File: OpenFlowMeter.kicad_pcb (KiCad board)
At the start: 2 copper layers, 70 x 28 mm, 92 parts, among them J1 Screw_Terminal_01x02, J2 Screw_Terminal_01x02, J3 Conn_01x06, J4 Conn_02x03_Odd_Even, J5 Conn_01x03, J6 Conn_02x04_Odd_Even, Q1 BC856, Q2 BC856, U1 LT1492, U2 STM32F103C8Tx, U3 LT1492, U4 R-78C3.3-1.0, U5 SN65HVD231, U6 LT1492, Y1 12 MHz

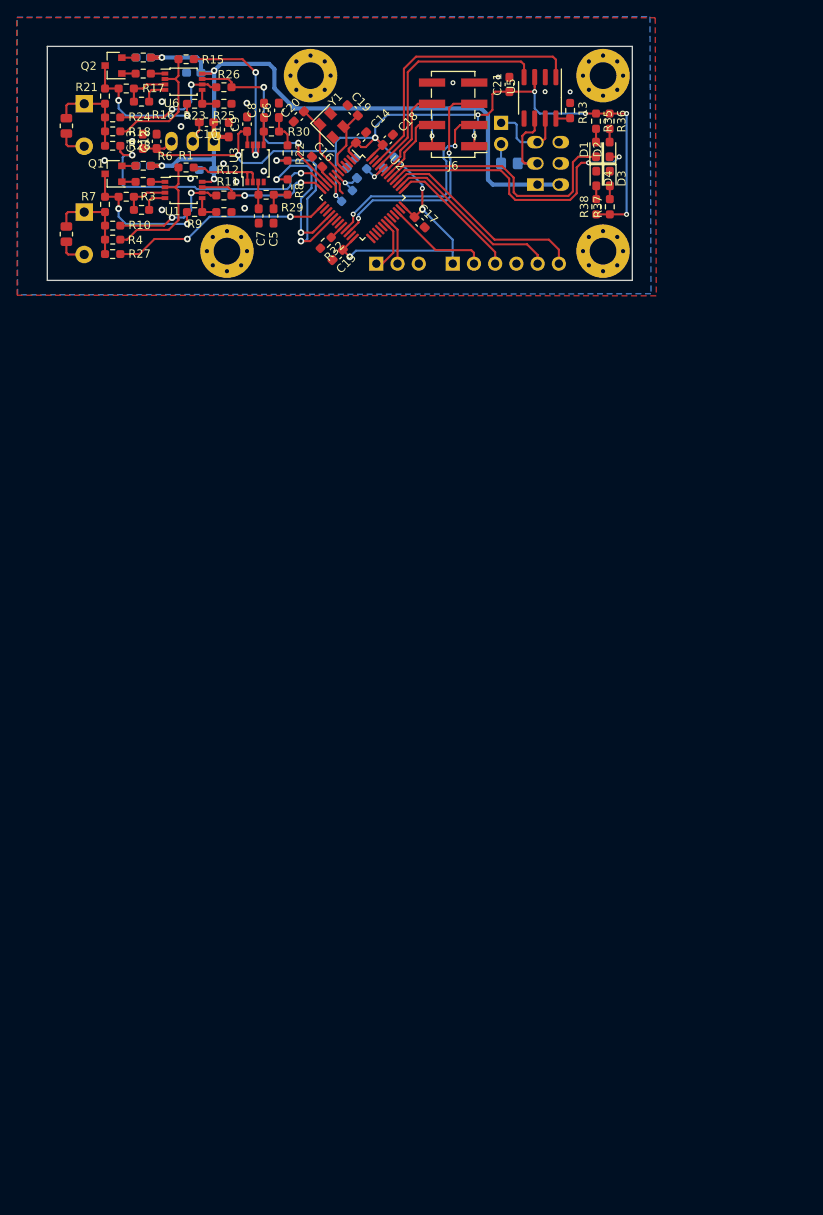
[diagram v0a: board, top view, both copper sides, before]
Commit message: BUGFIX footprint of LT1490
Footprint of LT1490 is SOIC8 and not Micro 8 -> had to enlarge the board.
At the same step, changed all footprints from handsolder to normal solder. (saves a little space)
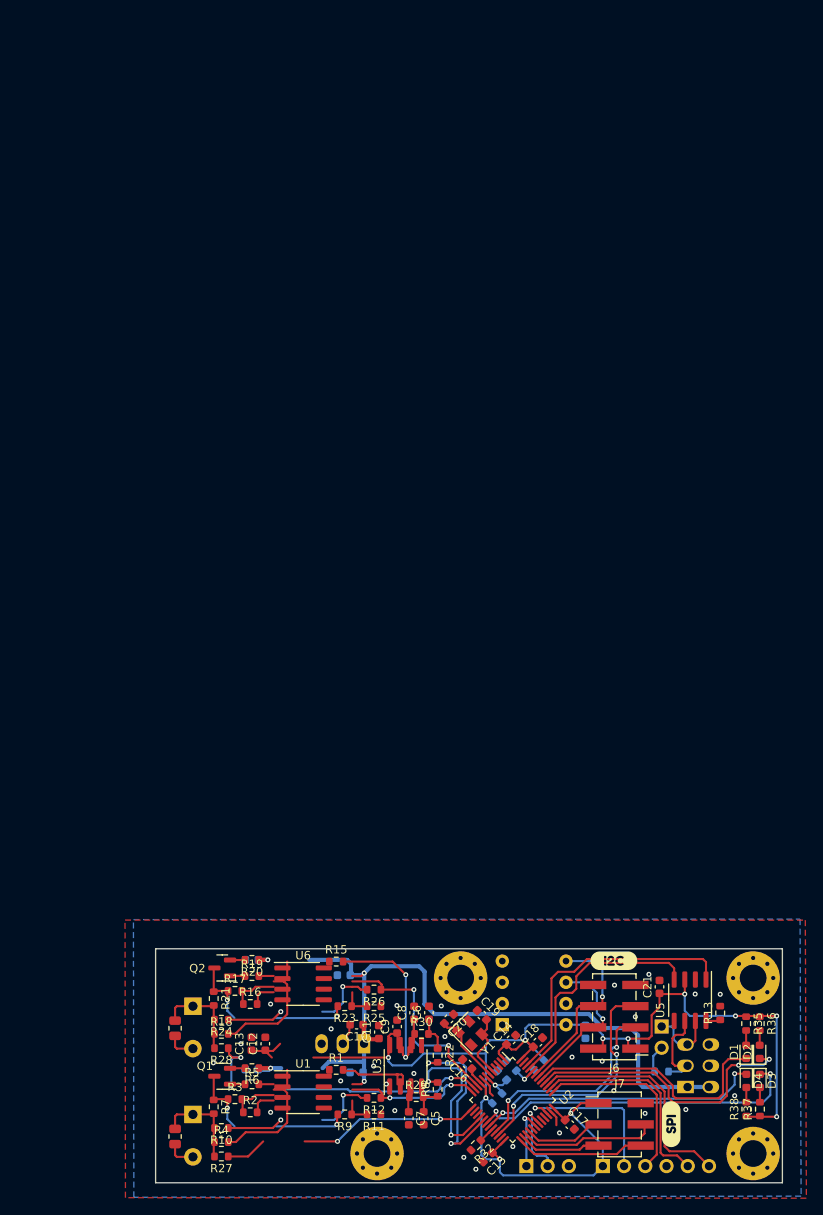
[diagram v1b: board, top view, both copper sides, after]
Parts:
- added C23: 100n, Capacitor_SMD:C_0603_1608Metric, B.Cu at (167.6, 92.7)
- added J7: Conn_02x03_Odd_Even, Connector_PinHeader_2.54mm:PinHeader_2x03_P2.54mm_Vertical_SMD, F.Cu at (171.7, 103.8)
- added U7: 24LC64, Package_DIP:DIP-8_W7.62mm, B.Cu at (157.6, 91.9)
- added kibuzzard-61DDB483: G***, kibuzzard-61DDB483, B.Cu at (173.6, 93.1)
- added kibuzzard-61DDB4E3: G***, kibuzzard-61DDB4E3, F.Cu at (177.8, 103.8)
- added kibuzzard-61DDB4F7: G***, kibuzzard-61DDB4F7, F.Cu at (171.0, 84.2)
- C1, C10, C11, C12, C13, C14, C15, C16, C17, C18, C19, C2, C20, C21, C22, C3, C4, C5, C6, C7, C8, C9: footprint Capacitor_SMD:C_0603_1608Metric_Pad1.08x0.95mm_HandSolder -> Capacitor_SMD:C_0603_1608Metric
- D1, D2, D3, D4: footprint LED_SMD:LED_0603_1608Metric_Pad1.05x0.95mm_HandSolder -> LED_SMD:LED_0603_1608Metric
- R1, R10, R11, R12, R13, R15, R16, R17, R18, R19, R2, R20, R21, R22, R23, R24, R25, R26, R27, R28, R29, R3, R30, R31, R32, R33, R34, R35, R36, R37, R38, R4, R5, R6, R7, R8, R9: footprint Resistor_SMD:R_0603_1608Metric_Pad0.98x0.95mm_HandSolder -> Resistor_SMD:R_0603_1608Metric
- R14: footprint Resistor_SMD:R_0805_2012Metric_Pad1.20x1.40mm_HandSolder -> Resistor_SMD:R_0603_1608Metric
- U1, U3, U6: footprint Package_SO:OnSemi_Micro8 -> Package_SO:SOIC-8_3.9x4.9mm_P1.27mm
- moved R14 110.2 mm to (176.7, 97.5)
- moved Y1 109.8 mm to (153.8, 92.8)
- moved JP1 109.8 mm to (176.7, 92.1)
- moved J6 109.7 mm to (171.0, 90.9)
- moved C10 109.5 mm to (140.2, 91.8)
- moved C14 109.5 mm to (158.7, 93.7)
- moved C15 109.5 mm to (155.9, 107.7)
- moved C16 109.5 mm to (153.4, 96.6)
- moved C2 109.5 mm to (140.2, 97.6)
- moved C20 109.5 mm to (151.2, 91.2), turned to -135 degrees
- moved C22 109.5 mm to (157.6, 97.9)
- moved C4 109.5 mm to (138.7, 85.9)
- moved C9 109.5 mm to (145.0, 92.1)
- moved D1 109.5 mm to (186.8, 95.1)
- moved D2 109.5 mm to (188.4, 95.1)
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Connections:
- D3 pad 1: unconnected-(D3-Pad1) -> /Controller/LED3
- D4 pad 1: unconnected-(D4-Pad1) -> /Controller/LED4
- U2 pad 18: unconnected-(U2-Pad18) -> /Controller/LED3
- U2 pad 19: unconnected-(U2-Pad19) -> /Controller/LED4
- U2 pad 25: unconnected-(U2-Pad25) -> /Controller/SPI_NSS
- U2 pad 26: unconnected-(U2-Pad26) -> /Controller/SPI_SCK
- U2 pad 27: unconnected-(U2-Pad27) -> /Controller/SPI_MISO
- U2 pad 28: unconnected-(U2-Pad28) -> /Controller/SPI_MOSI
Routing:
- net /Controller/LED3: track 0.00 -> 40.3 mm, vias 0 -> 2
- net /Controller/LED4: track 0.00 -> 34.1 mm, vias 0 -> 2
- net +3V3: track 157.1 -> 189.0 mm
- net /ISET 2: track 20.6 -> 0.00 mm, vias 2 -> 0
- net /Controller/SPI_MISO: track 0.00 -> 16.2 mm
- net /Controller/SPI_NSS: track 0.00 -> 15.9 mm
- net /Controller/I2C1_SDA: track 11.4 -> 22.1 mm, vias 0 -> 1
- net /Controller/SPI_SCK: track 0.00 -> 10.2 mm
- net /Controller/I2C1_SCL: track 9.01 -> 19.0 mm, vias 0 -> 1
- net /Controller/SPI_MOSI: track 0.00 -> 9.90 mm
- net /Controller/TMS_SWDIO: track 12.5 -> 19.2 mm, vias 0 -> 1
- net /Controller/TCK_SWCLK: track 16.2 -> 22.4 mm
- net /Controller/UART1_RX: track 5.58 -> 9.36 mm, vias 0 -> 1
- net /Controller/TDI: track 21.7 -> 25.3 mm
- net Net-(C8-Pad1): track 3.39 -> 0.00 mm
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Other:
- board size 70 x 28 mm -> 75 x 28 mm

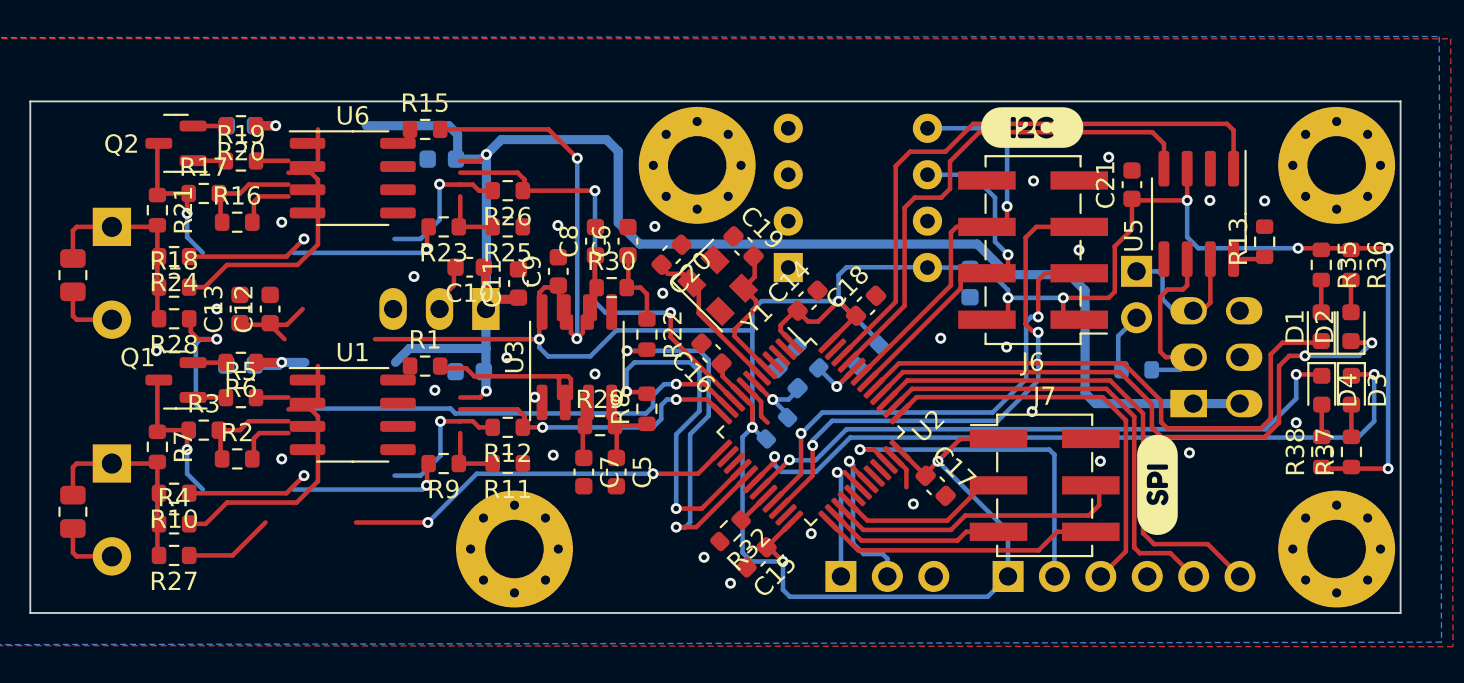
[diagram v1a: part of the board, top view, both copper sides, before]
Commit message: fixed layout
Fixed layout to host lager amplifier footprints.
Still some DRC warnings, but mostly regarding Silkscreen / Soldermask issues.
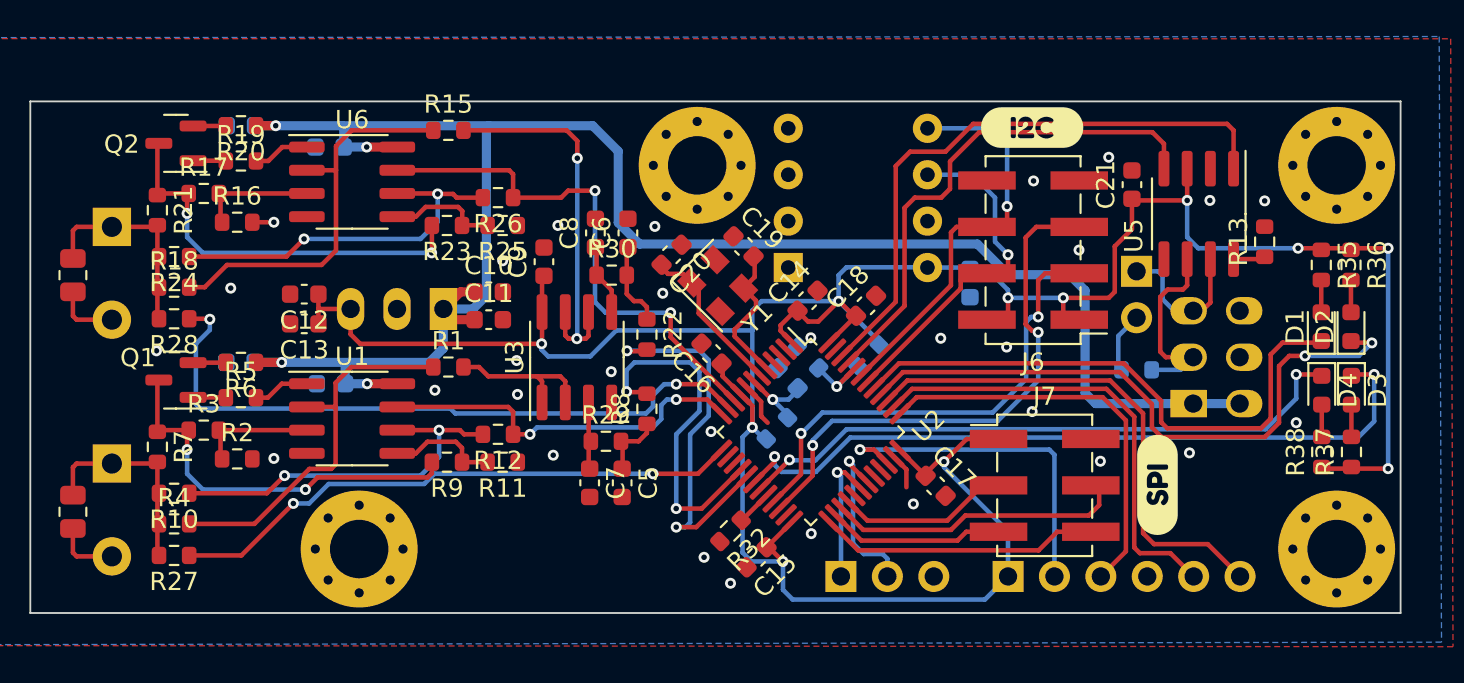
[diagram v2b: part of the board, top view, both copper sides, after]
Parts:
- moved H1 8.50 mm to (134.1, 107.3)
- moved C2 7.62 mm to (132.6, 98.2)
- moved C4 6.18 mm to (132.5, 85.3)
- moved C13 3.61 mm to (131.1, 94.9), turned to 180 degrees
- moved C11 2.56 mm to (141.2, 94.7), turned to 0 degrees
- moved U4 2.33 mm to (138.7, 94.1)
- moved C12 2.04 mm to (131.1, 93.3), turned to 180 degrees
- moved C10 1.70 mm to (141.2, 93.2), turned to 0 degrees
- moved R1 1.27 mm to (139.0, 97.3)
- moved R15 1.27 mm to (139.0, 84.4)
- moved C9 0.95 mm to (144.2, 91.5)
- moved R29 0.91 mm to (147.6, 101.4)
- moved R30 0.68 mm to (148.0, 92.3)
- moved C5 0.67 mm to (148.5, 103.6)
- moved C7 0.67 mm to (146.8, 103.6)
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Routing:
- net +3V3: track 189.0 -> 160.6 mm, vias 13 -> 11
- net /ISET 2: track 0.00 -> 21.3 mm, vias 0 -> 2
- net +24V: track 96.6 -> 105.0 mm
- net GND: track 20.6 -> 12.9 mm, vias 28 -> 30
- net Net-(R10-Pad1): track 14.4 -> 20.7 mm
- net Net-(R24-Pad1): track 14.4 -> 20.6 mm
- net Net-(R15-Pad1): track 15.8 -> 21.8 mm
- net Net-(Q2-Pad3): track 16.6 -> 22.0 mm
- net Net-(R1-Pad1): track 15.8 -> 21.1 mm
- net /U1: track 26.5 -> 31.4 mm
- net Net-(Q1-Pad3): track 16.6 -> 21.5 mm
- net /I2: track 24.9 -> 29.1 mm
- net /I1: track 16.5 -> 20.6 mm
- net /U2: track 32.8 -> 36.9 mm
- net Net-(C8-Pad1): track 0.00 -> 3.83 mm
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
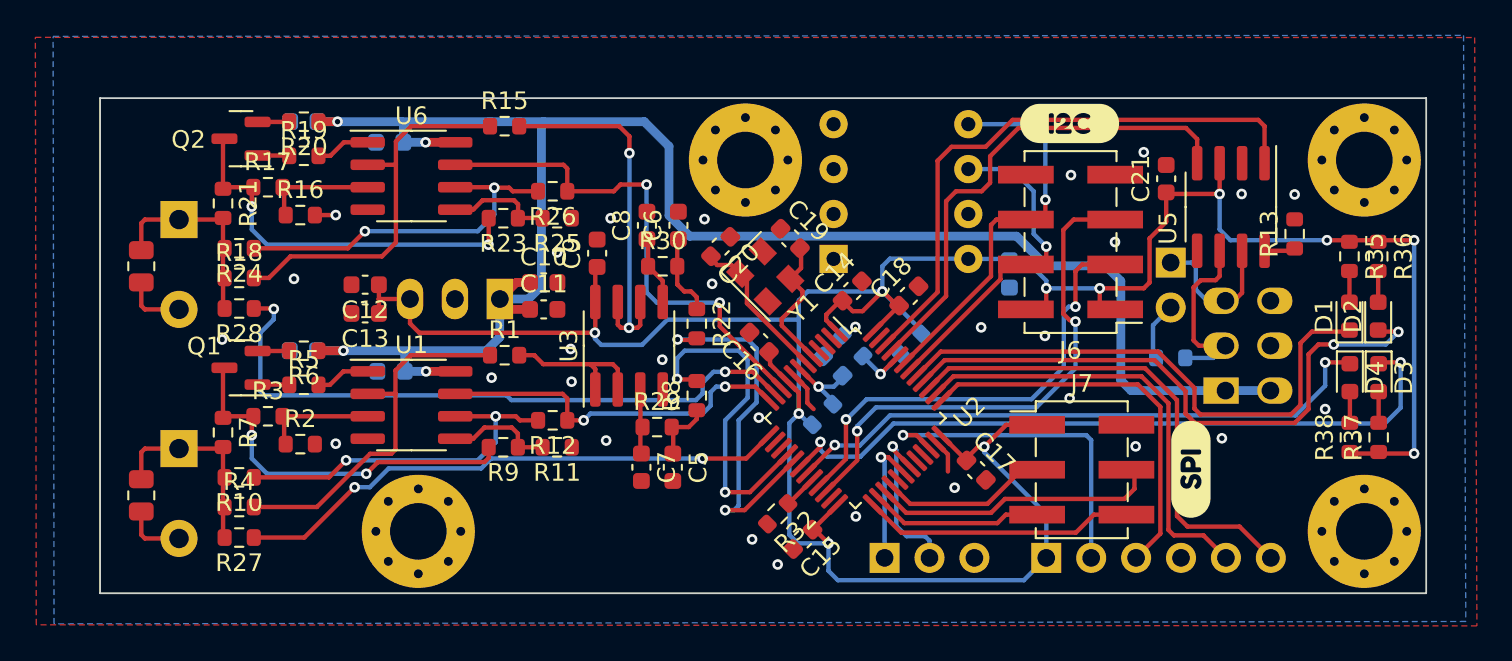
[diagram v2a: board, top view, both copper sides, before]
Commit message: board DRC clean
removed all DRC warnings / errors
had to waive some because Silkscreen is colliding with Board Edges and components are placed too close to footprints. (SMD pin header)
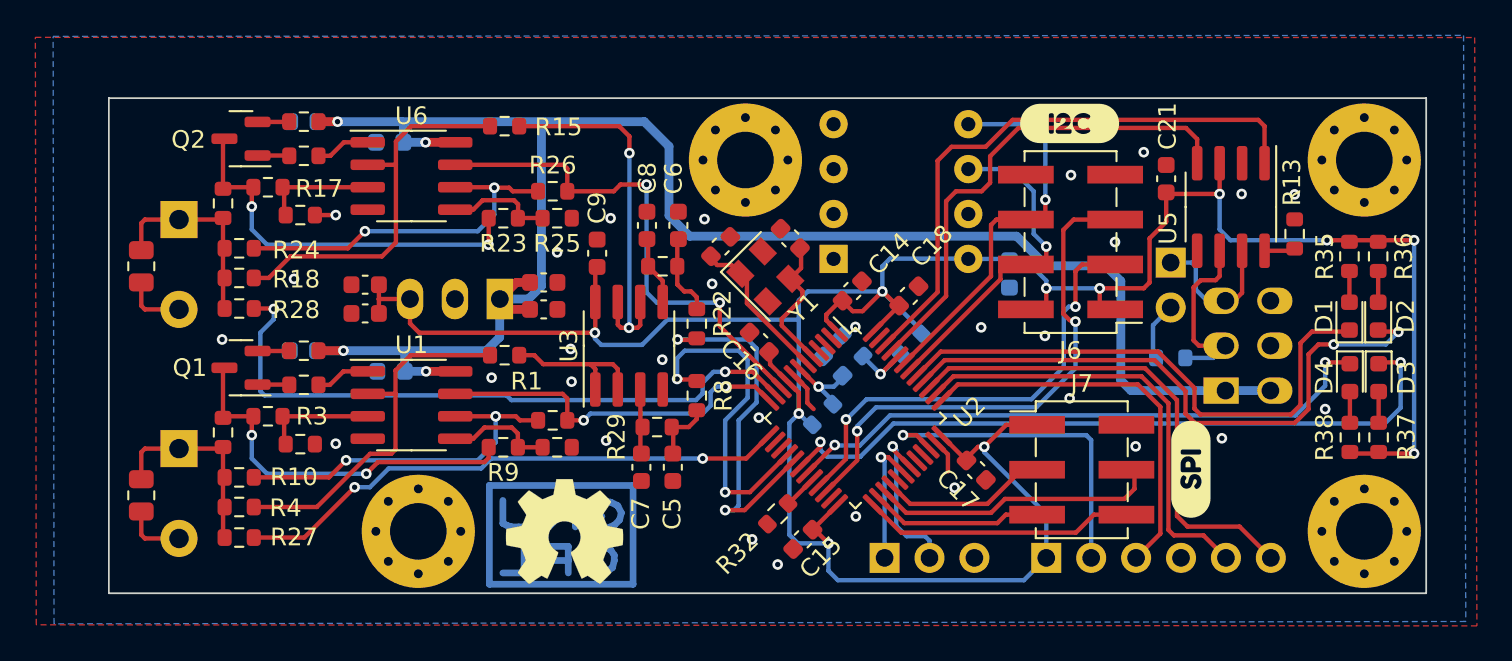
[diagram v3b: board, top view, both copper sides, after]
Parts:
- added REF**: OSHW-Symbol_6.7x6mm_SilkScreen, Symbol:OSHW-Symbol_6.7x6mm_SilkScreen, F.Cu at (142.4, 107.3)
- added REF**: KiCad-Logo2_6mm_SilkScreen, Symbol:KiCad-Logo2_6mm_SilkScreen, B.Cu at (150.6, 105.7)
- added REF**: Symbol_GNU-GPL_CopperTop_Small, Symbol:Symbol_GNU-GPL_CopperTop_Small, B.Cu at (142.2, 107.7)
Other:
- board size 75 x 28 mm -> 74.5 x 28 mm
- board text added: "JS2022"
- board text added: "OpenFlowMeter"
